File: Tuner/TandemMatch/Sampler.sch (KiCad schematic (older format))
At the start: 62 parts, among them J43 Conn_01x02, J44 Conn_Coaxial, J45 Conn_01x01, J46 Conn_01x01, J47 Conn_01x01, J48 Conn_01x01, J49 Conn_01x01, J50 Conn_01x01, J51 Conn_01x01, J52 Conn_01x01, J53 Conn_01x01, J54 Conn_01x02, J55 Conn_01x01, J56 Conn_01x01, J57 Conn_01x01, J58 Conn_01x02, J59 Conn_Coaxial, J60 Conn_01x01, J61 Conn_01x01, J62 Conn_01x01, J63 Conn_01x01, J64 Conn_01x01, J65 Conn_01x01, J66 Conn_01x01, J67 Conn_01x01, J68 Conn_01x02, J69 Conn_01x01, J70 Conn_01x01, J71 Conn_01x01, J72 Conn_01x01, J73 Conn_01x02, J74 Conn_01x02, J75 Conn_01x02, J76 Conn_01x02, J77 Conn_01x01, J80 Conn_01x01, J81 Conn_01x01

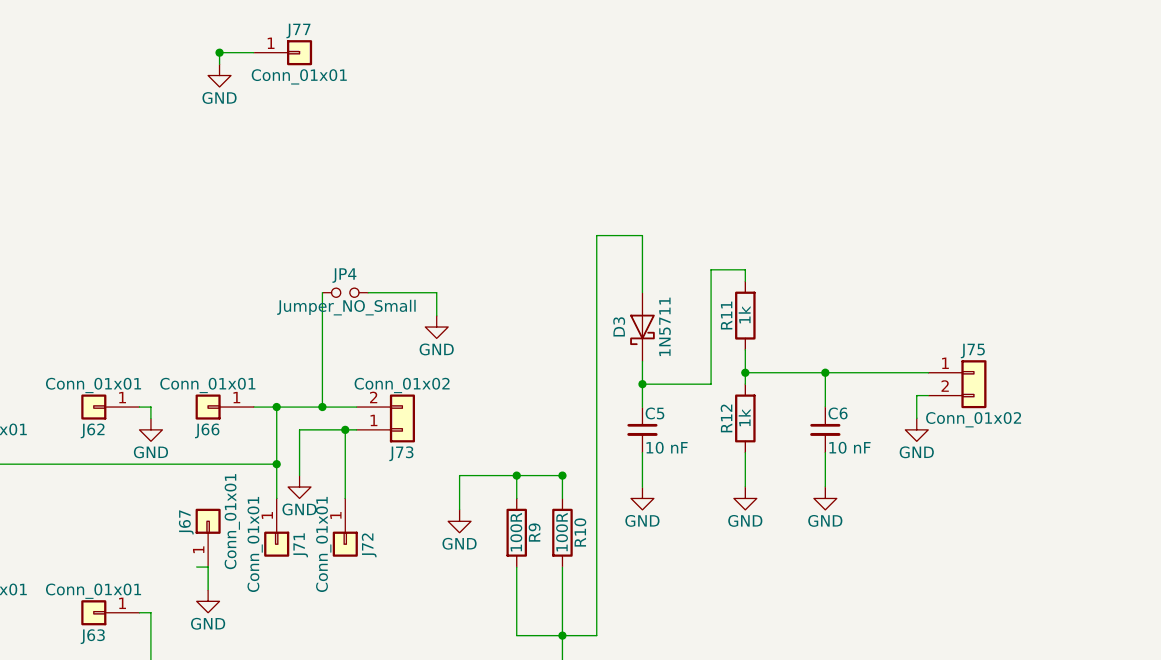
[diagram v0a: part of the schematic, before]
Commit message: TandemMatch to JLCPCB
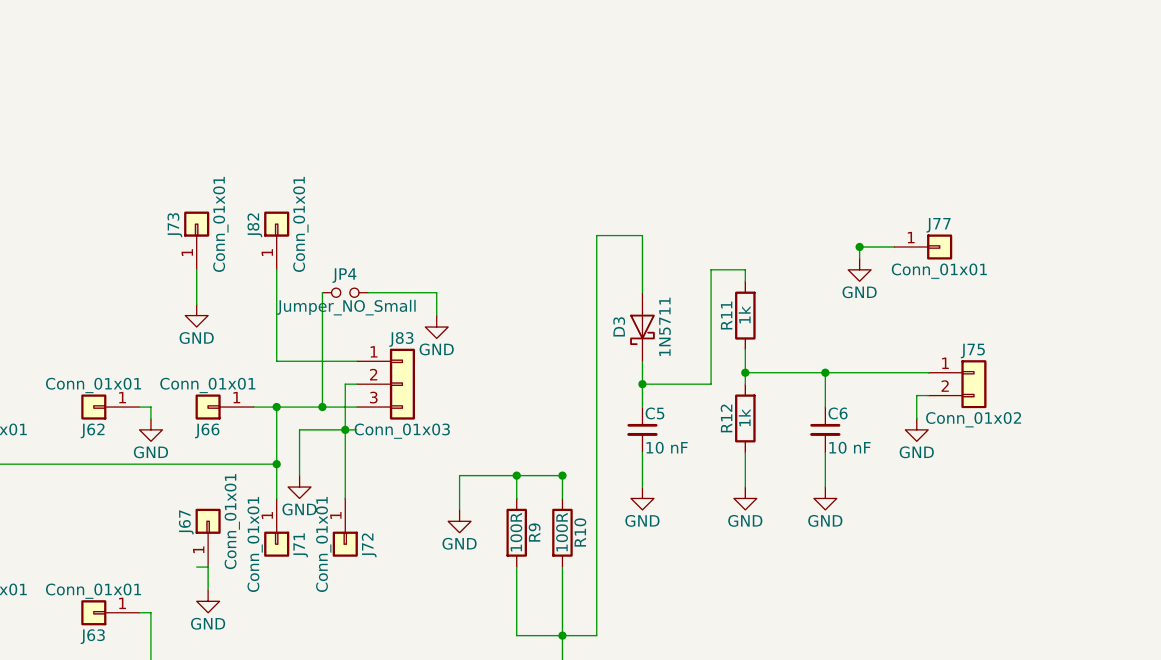
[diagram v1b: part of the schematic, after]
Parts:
- removed J73: Conn_01x02, Connectors_Terminal_Blocks:TerminalBlock_bornier-2_P5.08mm, symbol Conn_01x02
- added J73, J82: Conn_01x01, Connectors:1pin, symbol Conn_01x01
- added J83: Conn_01x03, Connectors_Terminal_Blocks:TerminalBlock_bornier-3_P5.08mm, symbol Conn_01x03
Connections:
- net GND: now also J73.1 (Pin_1), J83.2 (Pin_2)
- net at J66.1 (Pin_1), J71.1 (Pin_1), JP3.1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: now also J83.3 (Pin_3)
- new net: J82.1 (Pin_1), J83.1 (Pin_1)
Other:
- moved on the sheet: J77
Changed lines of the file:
@@
 $EndComp
 $Comp
-L GND #PWR36
+L GND #PWR37
 U 1 1 5C6A6080
 P 6700 3450
-F 0 "#PWR36" H 6700 3200 50  0001 C CNN
+F 0 "#PWR37" H 6700 3200 50  0001 C CNN
 F 1 "GND" H 6700 3300 50  0000 C CNN
 F 2 "" H 6700 3450 50  0001 C CNN
@@
 $EndComp
 $Comp
-L Conn_01x02 J73
-U 1 1 5C6A63C1
-P 7550 2750
-F 0 "J73" H 7550 2850 50  0000 C CNN
-F 1 "Conn_01x02" H 7550 2550 50  0000 C CNN
-F 2 "Connectors_Terminal_Blocks:TerminalBlock_bornier-2_P5.08mm" H 7550 2750 50  0001 C CNN
-F 3 "" H 7550 2750 50  0001 C CNN
-	1    7550 2750
-	1    0    0    1
-$EndComp
-$Comp
 L GND #PWR38
 U 1 1 5C6A6505
@@
 $EndComp
 $Comp
-L GND #PWR49
+L GND #PWR50
 U 1 1 5C6A99AD
 P 9800 5450
-F 0 "#PWR49" H 9800 5200 50  0001 C CNN
+F 0 "#PWR50" H 9800 5200 50  0001 C CNN
 F 1 "GND" H 9800 5300 50  0000 C CNN
 F 2 "" H 9800 5450 50  0001 C CNN
@@
 Connection ~ 4650 2650
 Wire Wire Line
-	7300 2750 7300 3050
+	7300 2550 7300 3050
 Connection ~ 7300 2750
 Wire Wire Line
@@
 $EndComp
 $Comp
-L GND #PWR48
+L GND #PWR49
 U 1 1 5C6ABF0C
 P 9800 2700
-F 0 "#PWR48" H 9800 2450 50  0001 C CNN
+F 0 "#PWR49" H 9800 2450 50  0001 C CNN
 F 1 "GND" H 9800 2550 50  0000 C CNN
 F 2 "" H 9800 2700 50  0001 C CNN
@@
 $EndComp
 $Comp
-L GND #PWR50
+L GND #PWR51
 U 1 1 5C6AC29E
 P 10550 5150
-F 0 "#PWR50" H 10550 4900 50  0001 C CNN
+F 0 "#PWR51" H 10550 4900 50  0001 C CNN
 F 1 "GND" H 10550 5000 50  0000 C CNN
 F 2 "" H 10550 5150 50  0001 C CNN
@@
 L Conn_01x01 J77
 U 1 1 5C6AD17A
-P 7100 1100
-F 0 "J77" H 7100 1200 50  0000 C CNN
-F 1 "Conn_01x01" H 7100 1000 50  0000 C CNN
-F 2 "Pin_Headers:Pin_Header_Straight_1x01_Pitch2.54mm" H 7100 1100 50  0001 C CNN
-F 3 "" H 7100 1100 50  0001 C CNN
-	1    7100 1100
-	1    0    0    -1
-$EndComp
-$Comp
-L GND #PWR37
+P 9900 1950
+F 0 "J77" H 9900 2050 50  0000 C CNN
+F 1 "Conn_01x01" H 9900 1850 50  0000 C CNN
+F 2 "Pin_Headers:Pin_Header_Straight_1x01_Pitch2.54mm" H 9900 1950 50  0001 C CNN
+F 3 "" H 9900 1950 50  0001 C CNN
+	1    9900 1950
+	1    0    0    -1
+$EndComp
+$Comp
+L GND #PWR48
 U 1 1 5C6AD181
-P 6750 1150
-F 0 "#PWR37" H 6750 900 50  0001 C CNN
-F 1 "GND" H 6750 1000 50  0000 C CNN
-F 2 "" H 6750 1150 50  0001 C CNN
-F 3 "" H 6750 1150 50  0001 C CNN
-	1    6750 1150
-	1    0    0    -1
-$EndComp
-Wire Wire Line
-	6750 1100 6900 1100
-Connection ~ 6750 1100
-Wire Wire Line
-	6750 1150 6750 1100
+P 9550 2000
+F 0 "#PWR48" H 9550 1750 50  0001 C CNN
+F 1 "GND" H 9550 1850 50  0000 C CNN
+F 2 "" H 9550 2000 50  0001 C CNN
+F 3 "" H 9550 2000 50  0001 C CNN
+	1    9550 2000
+	1    0    0    -1
+$EndComp
+Wire Wire Line
+	9550 1950 9700 1950
+Connection ~ 9550 1950
+Wire Wire Line
+	9550 2000 9550 1950
 $Comp
 L Jumper_NO_Small JP4
@@
 	1    0    0    -1
 $EndComp
+$Comp
+L Conn_01x03 J83
+U 1 1 5C6ADA43
+P 7550 2550
+F 0 "J83" H 7550 2750 50  0000 C CNN
+F 1 "Conn_01x03" H 7550 2350 50  0000 C CNN
+F 2 "Connectors_Terminal_Blocks:TerminalBlock_bornier-3_P5.08mm" H 7550 2550 50  0001 C CNN
+F 3 "" H 7550 2550 50  0001 C CNN
+	1    7550 2550
+	1    0    0    -1
+$EndComp
+$Comp
+L Conn_01x01 J82
+U 1 1 5C6ADD84
+P 7000 1850
+F 0 "J82" H 7000 1950 50  0000 C CNN
+F 1 "Conn_01x01" H 7000 1750 50  0000 C CNN
+F 2 "Connectors:1pin" H 7000 1850 50  0001 C CNN
+F 3 "" H 7000 1850 50  0001 C CNN
+	1    7000 1850
+	0    -1   -1   0
+$EndComp
+$Comp
+L Conn_01x01 J73
+U 1 1 5C6ADFAA
+P 6650 1850
+F 0 "J73" H 6650 1950 50  0000 C CNN
+F 1 "Conn_01x01" H 6650 1750 50  0000 C CNN
+F 2 "Connectors:1pin" H 6650 1850 50  0001 C CNN
+F 3 "" H 6650 1850 50  0001 C CNN
+	1    6650 1850
+	0    -1   -1   0
+$EndComp
+$Comp
+L GND #PWR36
+U 1 1 5C6AE0A5
+P 6650 2200
+F 0 "#PWR36" H 6650 1950 50  0001 C CNN
+F 1 "GND" H 6650 2050 50  0000 C CNN
+F 2 "" H 6650 2200 50  0001 C CNN
+F 3 "" H 6650 2200 50  0001 C CNN
+	1    6650 2200
+	1    0    0    -1
+$EndComp
+Wire Wire Line
+	6650 2200 6650 2050
+Wire Wire Line
+	7000 2050 7000 2450
+Wire Wire Line
+	7000 2450 7350 2450
+Wire Wire Line
+	7300 2550 7350 2550
 $EndSCHEMATC

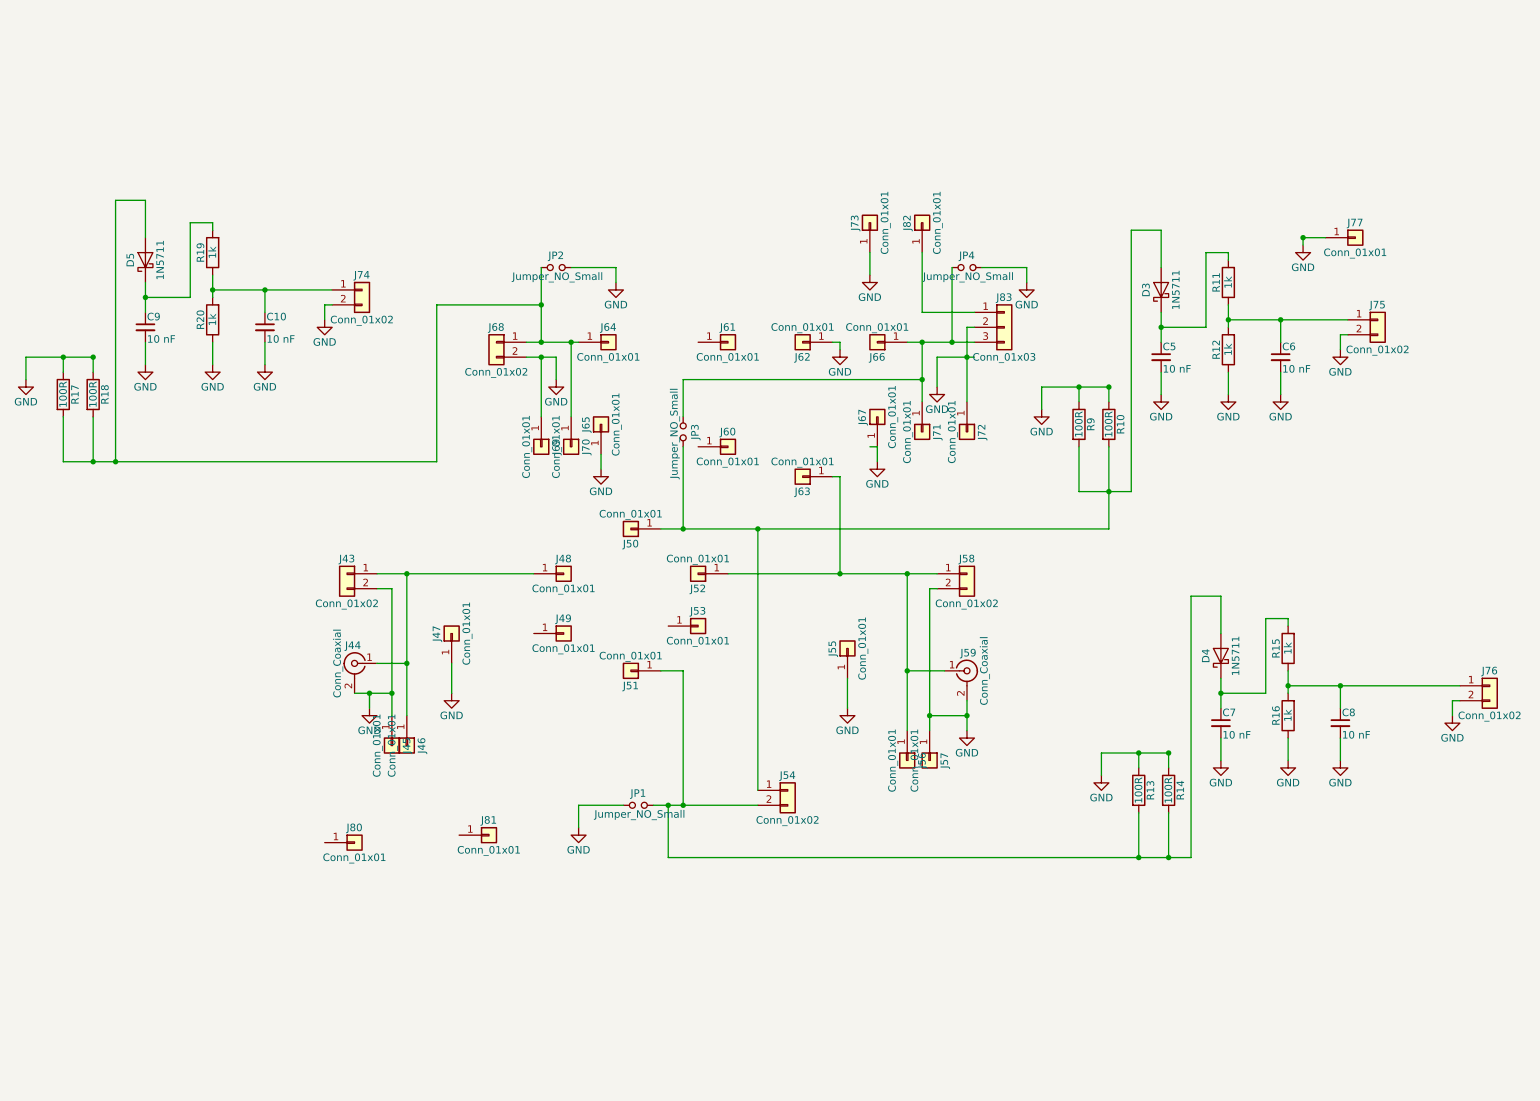
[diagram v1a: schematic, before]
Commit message: Added new DelayLine board, modified TandemMatch
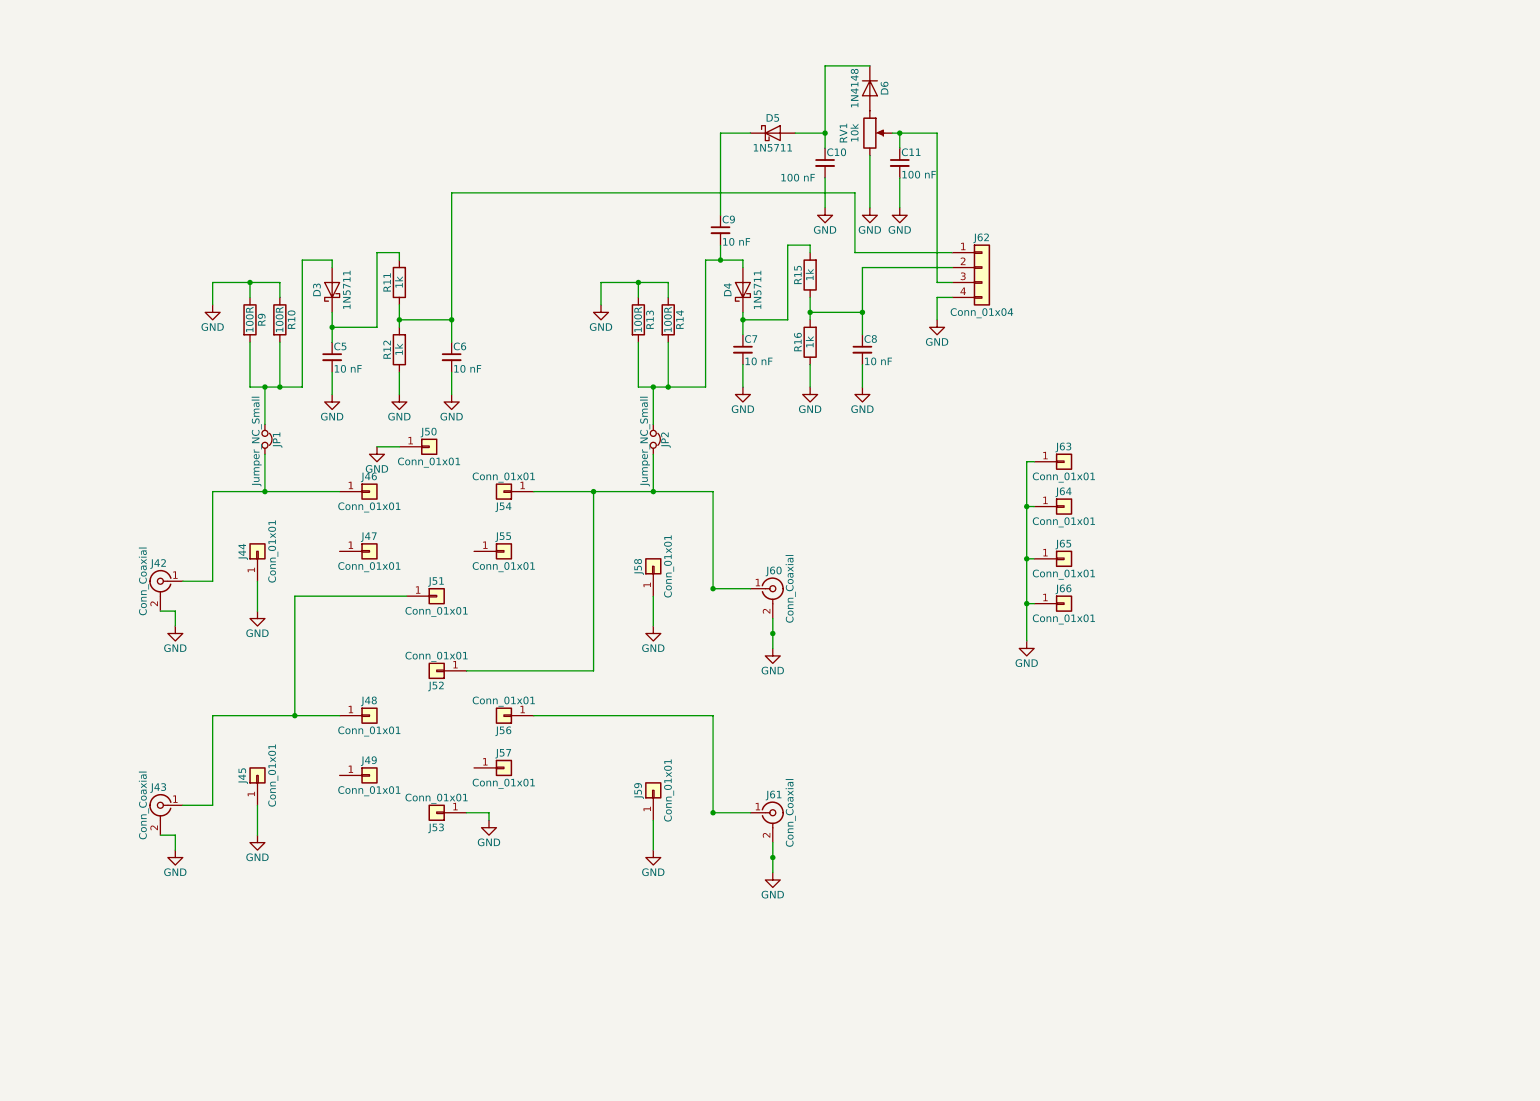
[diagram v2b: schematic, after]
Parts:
- removed J43, J54, J58, J68: Conn_01x02, Connectors_Terminal_Blocks:TerminalBlock_bornier-2_P5.08mm, symbol Conn_01x02
- removed J44, J59: Conn_Coaxial, TandemMatch:bnc_90_1-1337543-0, symbol Conn_Coaxial
- removed J60, J61, J62, J67, J69, J70, J71, J72, J73, J80, J81, J82: Conn_01x01, Connectors:1pin, symbol Conn_01x01
- removed J74, J75, J76: Conn_01x02, Pin_Headers:Pin_Header_Straight_1x02_Pitch2.54mm, symbol Conn_01x02
- removed J77: Conn_01x01, Pin_Headers:Pin_Header_Straight_1x01_Pitch2.54mm, symbol Conn_01x01
- removed J83: Conn_01x03, Connectors_Terminal_Blocks:TerminalBlock_bornier-3_P5.08mm, symbol Conn_01x03
- removed JP1, JP2, JP3, JP4: Jumper_NO_Small, Pin_Headers:Pin_Header_Straight_1x02_Pitch2.54mm, symbol Jumper_NO_Small
- removed R17, R18: 100R, Resistors_THT:R_Axial_DIN0309_L9.0mm_D3.2mm_P12.70mm_Horizontal, symbol R
- removed R19, R20: 1k, Resistors_THT:R_Axial_DIN0207_L6.3mm_D2.5mm_P7.62mm_Horizontal, symbol R
- added C11: 100 nF, Capacitors_THT:C_Disc_D5.0mm_W2.5mm_P5.00mm, symbol C_Small
- added D6: 1N4148, Diodes_THT:D_DO-41_SOD81_P7.62mm_Horizontal, symbol D
- added J42, J43, J60, J61: Conn_Coaxial, TandemMatch:bnc_90_1-1337543-0, symbol Conn_Coaxial
- added J44, J54, J58, J59: Conn_01x01, Connectors:1pin, symbol Conn_01x01
- added J62: Conn_01x04, Pin_Headers:Pin_Header_Straight_1x04_Pitch2.54mm, symbol Conn_01x04
- added JP1, JP2: Jumper_NC_Small, Pin_Headers:Pin_Header_Straight_1x02_Pitch2.54mm, symbol Jumper_NC_Small
- added RV1: 10k, Potentiometers:Potentiometer_Trimmer_Bourns_3296W, symbol POT
- C10: value 10 nF -> 100 nF
- R10, R13, R14, R9: footprint Resistors_THT:R_Axial_DIN0309_L9.0mm_D3.2mm_P12.70mm_Horizontal -> Resistors_THT:R_Axial_DIN0207_L6.3mm_D2.5mm_P7.62mm_Horizontal
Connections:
- net GND: now also J50.1 (Pin_1), J53.1 (Pin_1), J63.1 (Pin_1), J64.1 (Pin_1), J66.1 (Pin_1), C11.2, J42.2 (Ext), J43.2 (Ext), J44.1 (Pin_1), J58.1 (Pin_1), J59.1 (Pin_1), J60.2 (Ext), J61.2 (Ext), J62.4 (Pin_4), RV1.3; no longer C9.2, J47.1 (Pin_1), J55.1 (Pin_1), J57.1 (Pin_1)
- net at J46.1 (Pin_1): now also J42.1 (In), JP1.2; no longer J48.1 (Pin_1)
- net at D3.2 (A), R10.2, R9.2: now also JP1.1; no longer J50.1 (Pin_1)
- net at D4.2 (A), R13.2, R14.2: now also C9.2, JP2.1; no longer J51.1 (Pin_1)
- net at D5.2 (A): now also C10.1, D6.1 (K); no longer J64.1 (Pin_1)
- net at C6.1, R11.1, R12.2: now also J62.1 (Pin_1)
- net at C8.1, R15.1, R16.2: now also J62.2 (Pin_2)
- new net: J52.1 (Pin_1), J54.1 (Pin_1), J60.1 (In), JP2.2
- new net: J43.1 (In), J48.1 (Pin_1), J51.1 (Pin_1)
- new net: J56.1 (Pin_1), J61.1 (In)
- new net: C11.1, J62.3 (Pin_3), RV1.2
- new net: D6.2 (A), RV1.1

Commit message: Added more instrumentation to TandemMatch, fixed grounding issue
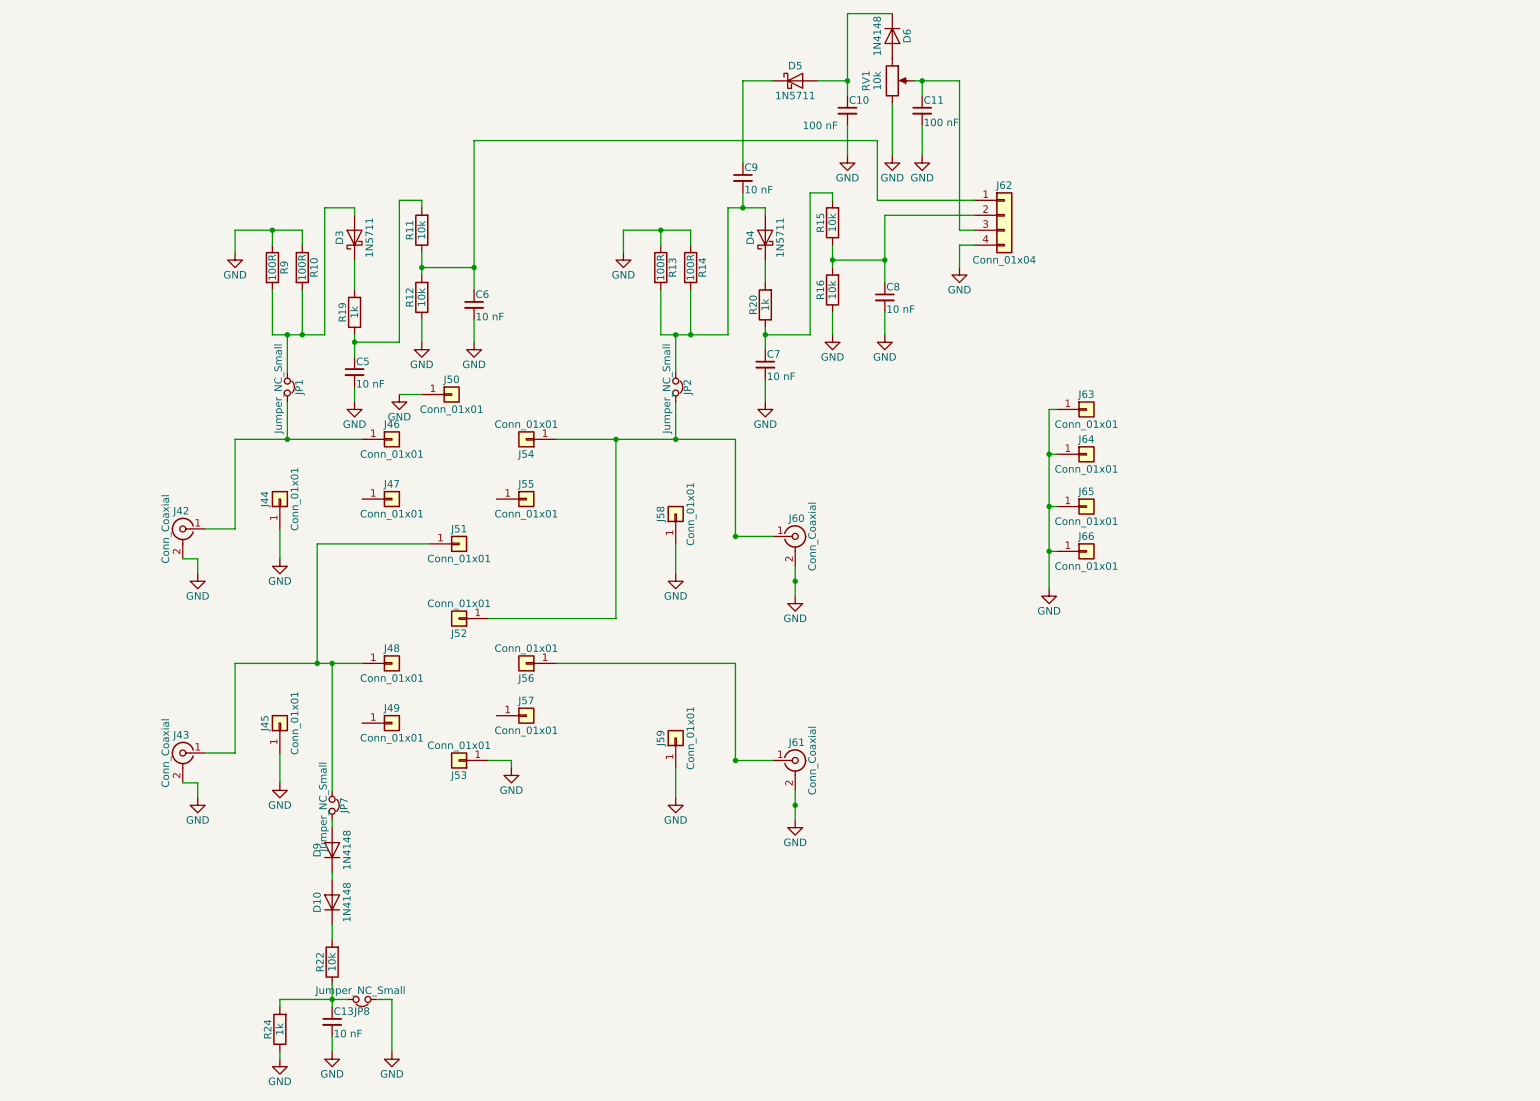
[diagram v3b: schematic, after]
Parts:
- added C13: 10 nF, Capacitors_THT:C_Disc_D5.0mm_W2.5mm_P2.50mm, symbol C_Small
- added D10, D9: 1N4148, Diodes_THT:D_DO-35_SOD27_P7.62mm_Horizontal, symbol D
- added JP7, JP8: Jumper_NC_Small, Pin_Headers:Pin_Header_Straight_1x02_Pitch2.54mm, symbol Jumper_NC_Small
- added R19, R20, R24: 1k, Resistors_THT:R_Axial_DIN0207_L6.3mm_D2.5mm_P7.62mm_Horizontal, symbol R
- added R22: 10k, Resistors_THT:R_Axial_DIN0207_L6.3mm_D2.5mm_P7.62mm_Horizontal, symbol R
- R11, R12, R15, R16: value 1k -> 10k
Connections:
- net GND: now also C13.2, JP8.1, R24.1
- net at J43.1 (In), J48.1 (Pin_1), J51.1 (Pin_1): now also JP7.1
- net at C5.1, R11.2: now also R19.1; no longer D3.1 (K)
- net at C7.1, R15.2: now also R20.1; no longer D4.1 (K)
- new net: D3.1 (K), R19.2
- new net: D4.1 (K), R20.2
- new net: D10.2 (A), D9.1 (K)
- new net: D9.2 (A), JP7.2
- new net: D10.1 (K), R22.2
- new net: C13.1, JP8.2, R22.1, R24.2
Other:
- moved on the sheet: C10, C11, C5, C6, C7, C8, C9, D3, D4, D5, D6, J42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
